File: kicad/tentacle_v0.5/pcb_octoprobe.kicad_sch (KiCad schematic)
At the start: 14 parts, among them J101 USB-226-BRW

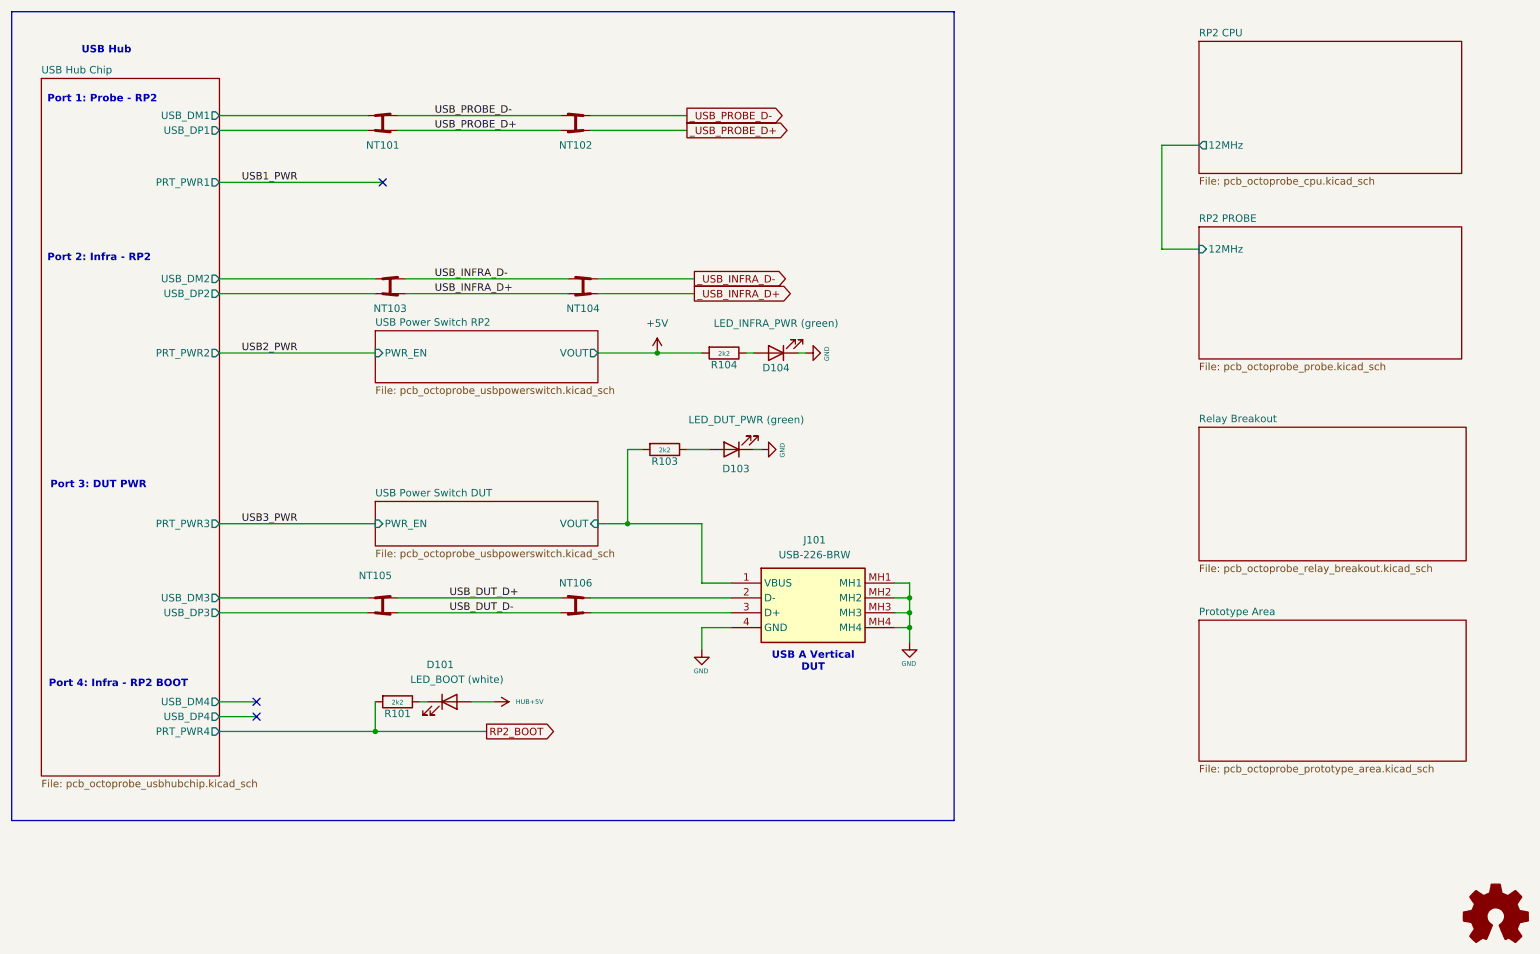
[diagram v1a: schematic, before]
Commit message: Breadboard: Remove pads from schematic
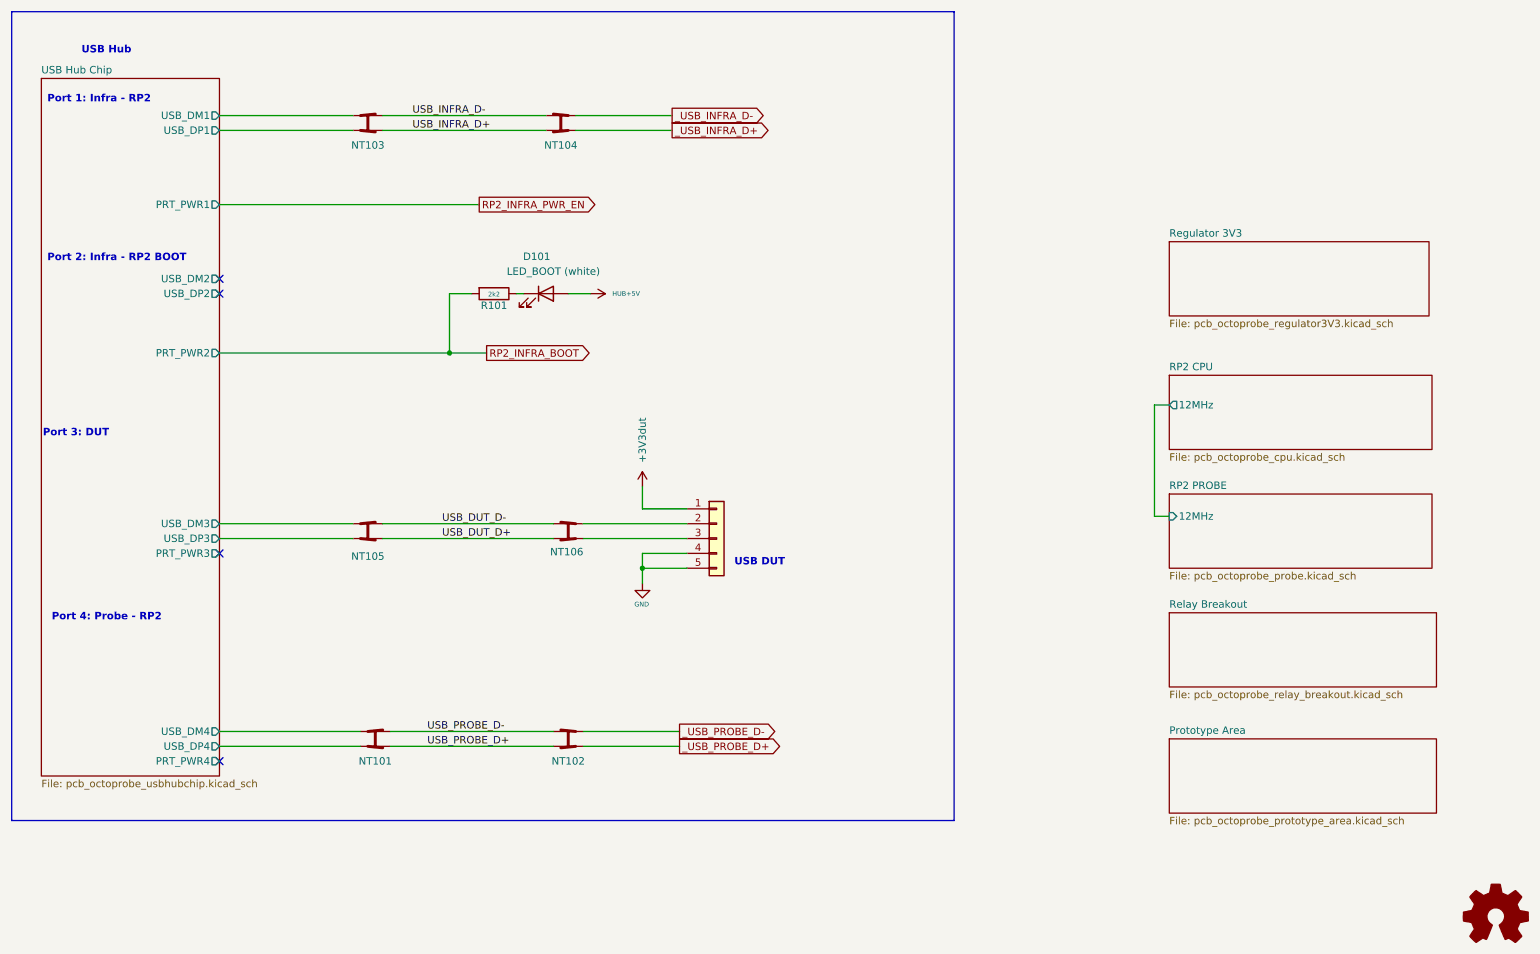
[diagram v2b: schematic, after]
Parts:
- removed D103, D104: green, LED_SMD:LED_0805_2012Metric, symbol 00_project_library:LED GREEN
- removed J101: USB-226-BRW, 00_project_library:USB226BRW, symbol 00_project_library:USB-226-BRW
- removed R103, R104: 2k2, Resistor_SMD:R_0805_2012Metric, symbol Device:R
- added J202: Conn_01x5, 00_project_library:PinSocket_1x5_P2.54mm_Vertical_squarepad_USB, symbol Connector_Generic:Conn_01x05
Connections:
- net GND: now also J202.4 (Pin_4), J202.5 (Pin_5)
- net USB Hub Chip/USB_DM1: now also NT103.3; no longer NT101.3
- net USB Hub Chip/USB_DM2: no longer NT103.3
- net USB Hub Chip/USB_DM3: now also NT105.3; no longer NT105.1
- net USB Hub Chip/USB_DM4: now also NT101.3
- net USB Hub Chip/USB_DP1: now also NT103.1; no longer NT101.1
- net USB Hub Chip/USB_DP2: no longer NT103.1
- net USB Hub Chip/USB_DP3: now also NT105.1; no longer NT105.3
- net USB Hub Chip/USB_DP4: now also NT101.1
- net at NT106.3: now also J202.3 (Pin_3)
- net at NT106.1: now also J202.2 (Pin_2)
- net RP2_BOOT renamed RP2_INFRA_BOOT
- new net +3V3dut: J202.1 (Pin_1)
- no-connect marks 3 -> 4
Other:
- removed sheet USB Power Switch DUT
- removed sheet USB Power Switch RP2
- added sheet Regulator 3V3 (pcb_octoprobe_regulator3V3.kicad_sch)
- note added: "Port 1: Infra - RP2"
- note added: "Port 2: Infra - RP2 BOOT"
- note added: "Port 3: DUT"
- note added: "Port 4: Probe - RP2"
- note added: "USB DUT"
- note removed: "Port 1: Probe - RP2"
- note removed: "Port 2: Infra - RP2"
- note removed: "Port 3: DUT PWR"
- note removed: "Port 4: Infra - RP2 BOOT"
- note removed: "USB A Vertical DUT"
- moved on the sheet: D101, NT101, NT102, NT103, NT104, NT105, NT106, R101

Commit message: Ordered tentacle v0.5 at jlcpcb
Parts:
- J202: now left out of the parts list
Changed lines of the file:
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@@
 	(title_block
 		(title "Octoprobe tentacle")
-		(date "2025-09-02")
+		(date "2025-08-31")
 		(rev "0.5")
 		(company "Hans Märki, Märki Informatik")
@@
 		(unit 1)
 		(exclude_from_sim no)
-		(in_bom yes)
+		(in_bom no)
 		(on_board yes)
 		(dnp no)
@@
 				)
 				(justify left)
-				(hide yes)
-			)
-		)
+			)
+		)
